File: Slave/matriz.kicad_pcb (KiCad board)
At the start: 2 copper layers, 32 parts, among them J1 Conn_01x05, J2 Conn_01x05, J3 Conn_01x08, J4 Conn_01x08, U1 MAX7219

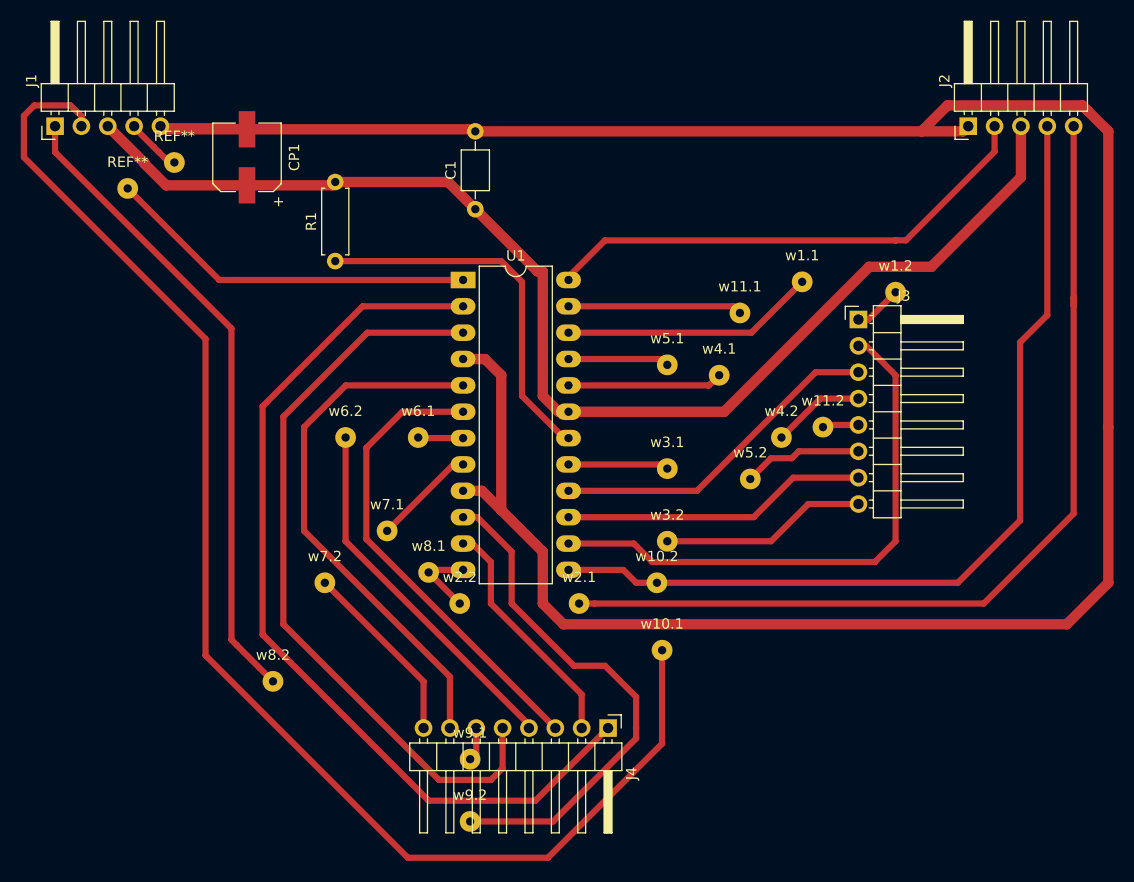
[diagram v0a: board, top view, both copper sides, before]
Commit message: finished the slave design and printed the mirrored final layout
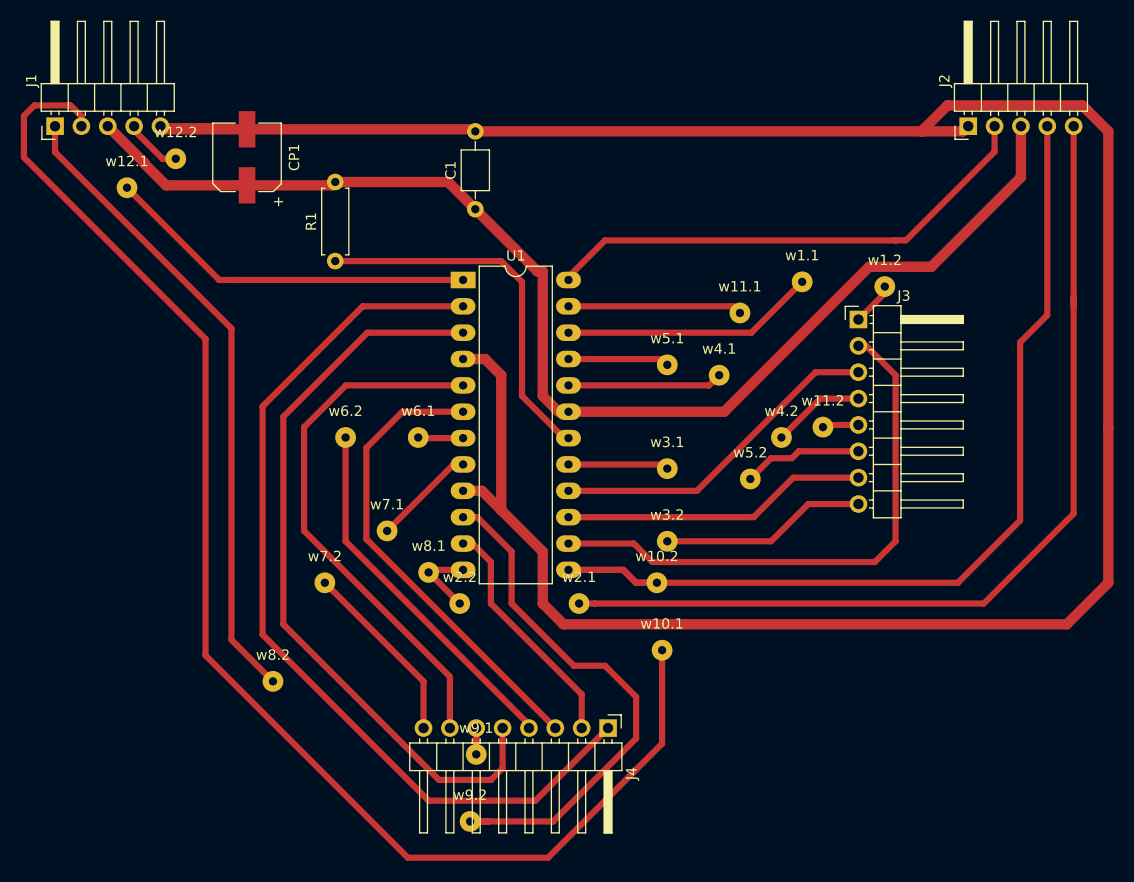
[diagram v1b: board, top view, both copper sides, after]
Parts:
- w12.1, w12.2: renamed from REF**; value SolderWirePad_single_0-8mmDrill -> (none)
- moved w1.2 1.17 mm to (188.0, 84.5)
- moved w9.1 0.75 mm to (148.6, 129.5)
- moved w12.2 0.39 mm to (119.6, 72.1)
- moved w12.1 0.10 mm to (114.9, 74.9)
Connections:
- w1.1 pad 1: (no net) -> /F7
- w1.2 pad 1: (no net) -> /F7
- w10.1 pad 1: (no net) -> /CLK
- w10.2 pad 1: (no net) -> /CLK
- w11.1 pad 1: (no net) -> /F3
- w11.2 pad 1: (no net) -> /F3
- w12.1 pad 1: (no net) -> /DIN
- w12.2 pad 1: (no net) -> /DIN
- w2.1 pad 1: (no net) -> /LD
- w2.2 pad 1: (no net) -> /LD
- w3.1 pad 1: (no net) -> /F0
- w3.2 pad 1: (no net) -> /F0
- w4.1 pad 1: (no net) -> /F4
- w4.2 pad 1: (no net) -> /F4
- w5.1 pad 1: (no net) -> /F2
- w5.2 pad 1: (no net) -> /F2
- w6.1 pad 1: (no net) -> /C3
- w6.2 pad 1: (no net) -> /C3
- w7.1 pad 1: (no net) -> /C7
- w7.2 pad 1: (no net) -> /C7
- w8.1 pad 1: (no net) -> /LD
- w8.2 pad 1: (no net) -> /LD
- w9.1 pad 1: (no net) -> /C5
- w9.2 pad 1: (no net) -> /C5
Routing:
- net (no net): track 18.9 -> 0.00 mm
- net /CLK: track 217.4 -> 226.4 mm
- net /LD: track 152.1 -> 159.9 mm
- net /C5: track 49.1 -> 56.0 mm
- net /C3: track 35.3 -> 39.7 mm
- net /F3: track 16.8 -> 20.3 mm
- net /F7: track 29.2 -> 28.3 mm
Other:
- net class Default: trace_width 1 -> 0.6
